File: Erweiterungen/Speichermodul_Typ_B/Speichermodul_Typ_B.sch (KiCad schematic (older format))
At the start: 12 parts, among them U15 DS8205D, U2 U2716 (U2732), U3 U6516D, X10 Sp.-Modul, X11 selects

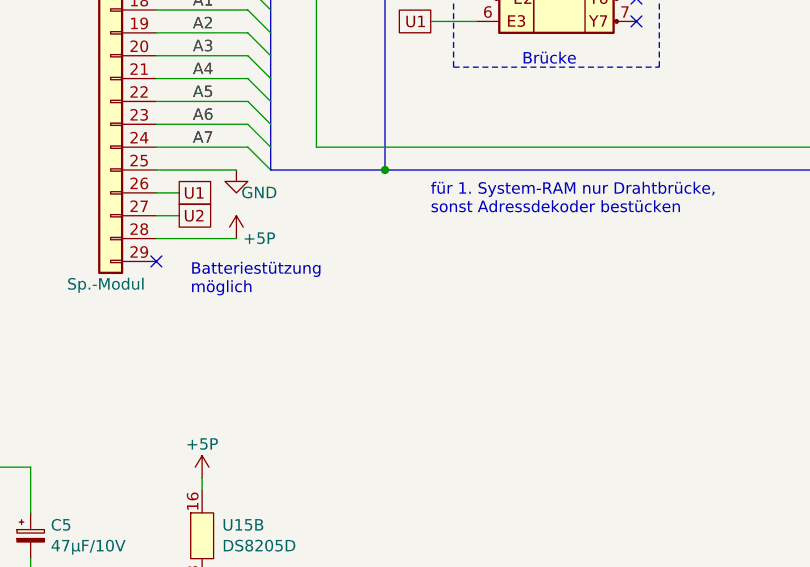
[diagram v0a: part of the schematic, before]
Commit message: Kommentar zur Spannungsversorgung
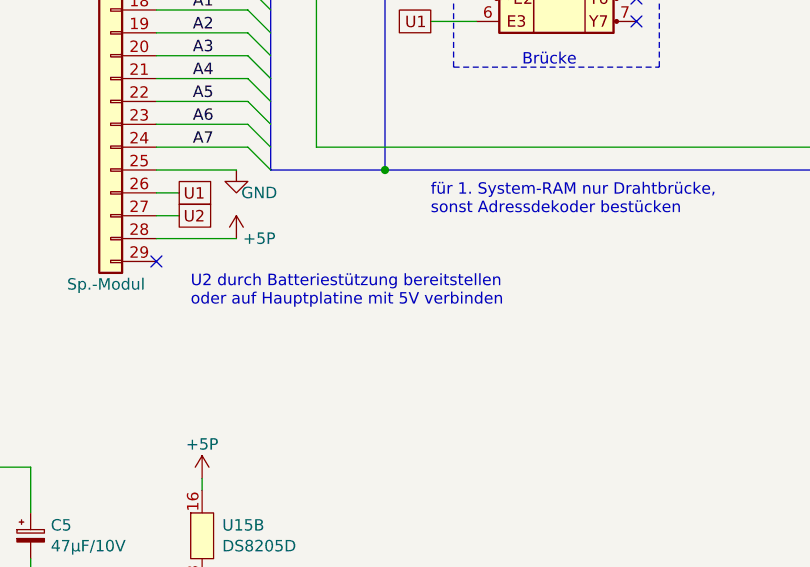
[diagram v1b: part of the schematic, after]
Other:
- note added: "U2 durch Batteriestützung bereitstellen\noder auf Hauptplatine mit 5V verbinden"
- note removed: "Batteriestützung\nmöglich"
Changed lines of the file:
@@
 Sheet 1 1
 Title "Speichermodul Typ B"
-Date "4.12.21"
-Rev "1"
+Date "14.12.21"
+Rev "2"
 Comp "Jugend+Technik"
 Comment1 "Bert"
@@
 Text Notes 6550 3700 0    50   ~ 0
 Auswahl\n2 kByte
-Text Notes 3700 5750 0    50   ~ 0
-Batteriestützung\nmöglich
+Text Notes 3700 5800 0    50   ~ 0
+U2 durch Batteriestützung bereitstellen\noder auf Hauptplatine mit 5V verbinden
 Text Notes 7450 3100 0    50   ~ 0
 2 kByte RAM-Speicher\n(max. 8 kByte)
@@
 Text Label 3750 2900 0    50   ~ 0
 ~CSB
-Wire Bus Line
-	4550 4050 4550 5200
-Wire Wire Line
-	9050 4650 9400 4650
-Wire Bus Line
-	8550 3950 8550 5200
-Wire Bus Line
-	7050 3550 7050 5200
-Wire Bus Line
-	10650 3950 10650 5200
-Wire Bus Line
-	9150 3550 9150 5200
-Wire Bus Line
-	4050 3200 4050 5200
 Text Notes 7850 7600 0    50   ~ 0
 Grundmodul 2k EPROM, 2k-8k RAM
+Wire Bus Line
+	4550 4050 4550 5200
+Wire Wire Line
+	9050 4650 9400 4650
+Wire Bus Line
+	8550 3950 8550 5200
+Wire Bus Line
+	7050 3550 7050 5200
+Wire Bus Line
+	10650 3950 10650 5200
+Wire Bus Line
+	9150 3550 9150 5200
+Wire Bus Line
+	4050 3200 4050 5200
 $EndSCHEMATC
